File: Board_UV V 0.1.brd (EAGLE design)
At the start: 100 x 80 mm, 32 parts, among them IC4 74HC14D, IC5 MAX3232CSE, U1 TLP521-4(GB), U2 TLP521-4(GB), U3 TLP521-4(GB)

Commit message: Add other component
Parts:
- added JP1, JP2: (no value), pinhead:1X08
- added JP3: (no value), pinhead:1X02
- added JP4: (no value), pinhead:1X16
- added JP5: (no value), pinhead:1X04
- added JP6: (no value), pinhead:1X06
- added JP7: (no value), pinhead:1X12
- added JP8: (no value), pinhead:1X03
- added LS1: BUZZER-PTH_KIT, SparkFun-Electromechanical:BUZZER-12MM-KIT
- added Q1, Q2: 500mA/300V, SparkFun-DiscreteSemi:SOT23-3
- added R21, R22: 2k2, SparkFun-Resistors:0603
- added R23, R25, R26, R27, R28, R29: 1k, SparkFun-Resistors:0603
- added R24: 10k, SparkFun-Resistors:0603
- added R30, R31, R32, R33, R34, R35: 330, SparkFun-Resistors:0603
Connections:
- new net 1A: JP2.4
- new net 1B: JP2.3
- new net 2A: JP2.5
- new net 2B: JP2.6
- new net BTN-1: U$1.A14
- new net BTN-2: U$1.D32
- new net BTN-3: U$1.D34
- new net BTN-4: U$1.D36
- new net BTN-5: U$1.D38
- new net BUZ-12V: U$1.D13
- new net BUZ-5V: U$1.D11
- new net DHT: U$1.D7
- new net DIR: JP1.8, U$1.D45
- new net EN: JP1.1, U$1.D43
- new net LCD-D11: U$1.A8
- new net LCD-D12: U$1.A10
- new net LCD-D2: U$1.A0
- new net LCD-D3: U$1.A2
- new net LCD-D4: U$1.A4
- new net LCD-D5: U$1.A6
- new net LED-1: U$1.D40
- new net LED-2: U$1.D42
- new net LED-3: U$1.D44
- new net LED-4: U$1.D46
- new net LED-5: U$1.D48
- new net LIM-B1: U$1.D22
- new net LIM-B2: U$1.D24
- new net LIM-B3: U$1.D26
- new net LIM-B4: U$1.D28
- new net LIM-CTR: U$1.D21
- new net LIM-S1: U$1.D30
- new net LIM-S2: U$1.D31
- new net MISO: JP1.2, U$1.D50
- new net MOSI: JP1.5, U$1.D51
- new net N$101: JP8.3
- new net N$25: Q1.1, R21.1
- new net N$41: R21.2, R22.2
- new net N$42: LS1.-, Q1.3
- new net N$66: Q2.1, R22.1
- new net N$67: JP3.2
- new net N$68: Q2.3
- new net N$69: R24.2, U2.5
- new net N$70: JP6.6, R25.1
- new net N$71: JP4.3, R23.1
- new net N$72: JP4.4
- new net N$73: JP5.2
- new net N$74: JP4.6
- new net N$75: JP5.3
- new net N$76: JP6.5, R26.1
- new net N$77: JP4.14
- new net N$78: JP4.13
- new net N$79: JP4.12
- new net N$80: JP4.11
- new net N$81: JP6.4, R27.1
- new net N$82: JP6.3, R28.1
- new net N$83: JP6.2, R29.1
- new net N$84: U2.12
- new net N$85: JP7.7, R33.2
- new net N$86: R24.1
- new net N$87: JP7.1, R30.2
- new net N$88: JP7.2
- new net N$89: JP7.3, R31.2
- new net N$90: JP7.4
- new net N$91: JP7.5, R32.2
- new net N$92: JP7.6
- new net N$93: JP7.8
- new net N$94: JP7.9, R34.2
- new net N$95: JP7.10
- new net N$96: JP7.11, R35.2
- new net N$97: JP7.12
- new net RL-1: U$1.D23
- new net RL-2: U$1.D25
- new net RL-3: U$1.D27
- new net RL-4: U$1.D29
- new net RX-DB9: U$1.D17
- new net RX-PWR: U$1.D19
- new net SCK: JP1.3, U$1.D52
- new net SPDT-1: U$1.D33
- new net SPDT-2: U$1.D35
- new net SPDT-3: U$1.D37
- new net SPDT-4: U$1.D39
- new net SPDT-5: U$1.D41
- new net SS: JP1.4, U$1.D53
- new net STEP: JP1.7, U$1.D49
- new net TX-DB9: U$1.D16
- new net TX-PWR: U$1.D18
- net GND: now also JP2.1, JP4.1, JP4.16, JP4.5, JP5.4, JP8.1, Q1.2, Q2.2, R25.2, R26.2, R27.2, R28.2, R29.2, U$1.GND.1, U$1.GND.2, U2.11
- net GND-ISO: now also JP2.7, U2.6
- net VCC: now also JP2.2, JP4.15, JP4.2, JP5.1, JP6.1, JP8.2, LS1.+, R23.2, R30.1, R31.1, R32.1, R33.1, R34.1, R35.1, U$1.+5V.1, U$1.+5V.2, U$1.VIN.1, U$1.VIN.2
- net VCC_2: now also JP2.8, JP3.1

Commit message: add board design
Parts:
- removed JP3: (no value), pinhead:1X02
- removed JP4: (no value), pinhead:1X16
- removed JP5: (no value), pinhead:1X04
- removed JP6: (no value), pinhead:1X06
- removed JP7: (no value), pinhead:1X12
- removed JP8: (no value), pinhead:1X03
- added DS1: LCM-S02004DSF, LCM-S02004DSF:LCMS02004DSF
- added H1, H2, H3, H4: MOUNT-PAD-SQUARE3.0, holes:3,0-PAD-SQUARE
- added IC1: 74HC14D, 74xx-eu:SO14
- added J2: POWER_JACK, SparkFun-Connectors:POWER_JACK_PTH
- added LED1, LED2, LED3, LED4, LED5, LED6: (no value), led:LED5MM
- added R36, R37, R38, R39, R41, R42: 1k, SparkFun-Resistors:0603
- added S1, S2, S3, S4, S5: MOMENTARY-SWITCH-SPST-PTH-12MM, SparkFun-Switches:TACTILE_SWITCH_PTH_12MM
- added U$2, U$3, U$4, U$5, U$6, U$7: ROCKER, rocker sw:320-916
- added U$8: DC-DC-STEP-DOWN-LM2596, diy-modules:DC-DC-STEP-DOWN-LM2596
- added X1: 22-23-2021, con-molex:22-23-2021
- added X2: 1751303, con-phoenix-350:1751303
- added X3: 1751277, con-phoenix-350:1751277
- added X4: 22-23-2031, con-molex:22-23-2031
- added X5: 22-23-2041, con-molex:22-23-2041
- added X6: 1751280, con-phoenix-350:1751280
- R23: value 1k -> 10k
- moved R31 350.4 mm to (130.7, 76.2)
- moved R24 317.5 mm to (146.2, 65.3), flipped to the bottom
- moved R33 300.8 mm to (117.9, 15.3)
- moved R26 294.1 mm to (21.1, 96.8), turned to 180 degrees
- moved R25 292.9 mm to (21.1, 99.2), turned to 180 degrees
- moved R29 290.9 mm to (99.1, 39.5), turned to 90 degrees
- moved R28 289.2 mm to (101.1, 39.5), turned to 90 degrees
- moved R35 287.6 mm to (41.9, 40.6), turned to 270 degrees
- moved R34 285.2 mm to (44.5, 40.6), turned to 270 degrees
- moved Q2 282.9 mm to (129.0, 56.3), flipped to the bottom, turned to 90 degrees
- moved R27 282.1 mm to (94.5, 39.5), turned to 270 degrees
- moved R32 280.6 mm to (49.5, 40.6), turned to 270 degrees
- moved R22 276.7 mm to (125.5, 56.2), flipped to the bottom, turned to 90 degrees
- moved R30 272.6 mm to (47.0, 40.6), turned to 270 degrees
- moved R23 260.1 mm to (84.6, 53.6), flipped to the bottom, turned to 90 degrees
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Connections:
- removed net N$101: JP8.3
- removed net N$11: R1.2
- removed net N$12: IC4.1, R2.2, U1.16
- removed net N$17: IC4.3, R3.2, U1.14
- removed net N$18: IC4.5, R5.1, U1.12
- removed net N$19: IC4.13, R6.1, U1.10
- removed net N$20: R4.1
- removed net N$21: R7.1
- removed net N$22: R8.1
- removed net N$26: R9.2
- removed net N$27: IC4.11, R10.2, U2.16
- removed net N$28: IC4.9, R11.2, U2.14
- removed net N$29: R13.1, U3.1
- removed net N$30: U3.15
- removed net N$31: U3.13
- removed net N$32: U3.11
- removed net N$34: U3.9
- removed net N$35: R16.2, U3.3
- removed net N$36: R19.2, U3.5
- removed net N$40: R12.1
- removed net N$41: R21.2, R22.2
- removed net N$43: R20.2, U3.7
- removed net N$44: IC4.8
- removed net N$45: IC4.10
- removed net N$46: IC4.12
- removed net N$50: IC4.2
- removed net N$51: IC4.4
- removed net N$52: IC4.6
- removed net N$67: JP3.2
- removed net N$68: Q2.3
- removed net N$70: JP6.6, R25.1
- removed net N$71: JP4.3, R23.1
- removed net N$72: JP4.4
- removed net N$73: JP5.2
- removed net N$74: JP4.6
- removed net N$75: JP5.3
- removed net N$76: JP6.5, R26.1
- removed net N$77: JP4.14
- removed net N$78: JP4.13
- removed net N$79: JP4.12
- removed net N$80: JP4.11
- removed net N$81: JP6.4, R27.1
- removed net N$82: JP6.3, R28.1
- removed net N$83: JP6.2, R29.1
- removed net N$84: U2.12
- removed net N$85: JP7.7, R33.2
- removed net N$86: R24.1
- removed net N$87: JP7.1, R30.2
- removed net N$88: JP7.2
- removed net N$90: JP7.4
- removed net N$92: JP7.6
- removed net N$93: JP7.8
- removed net N$95: JP7.10
- removed net N$97: JP7.12
- removed net VCC_2: JP2.8, JP3.1, R13.2, R16.1, R19.1, R20.1
- new net L-IN1: IC4.13, R2.2, U1.16
- new net L-IN2: IC4.11, R3.2, U1.14
- new net L-IN3: IC4.9, R5.1, U1.12
- new net L-IN4: IC4.1, R6.1, U1.10
- new net L-IN5: IC1.13, R10.2, U2.16
- new net L-IN6: IC1.11, R11.2, U2.14
- new net L-IN7: IC1.9, R23.2, U2.12
- new net L-O1: R1.2, X2.7
- new net L-O2: R4.1, X2.6
- new net L-O3: R7.1, X2.5
- new net L-O4: R8.1, X2.4
- new net L-O5: R9.2, X2.3
- new net L-O6: R12.1, X2.2
- new net L-O7: R24.1, X2.1
- new net LED-6: LED6.A, U$1.D48
- new net N$47: Q2.3, X1.2
- new net N$56: DS1.3, R36.1
- new net R-O1: U3.15, X3.5
- new net R-O2: U3.13, X3.4
- new net R-O3: U3.11, X3.3
- new net R-O4: U3.9, X3.2
- new net VCC-ISO: J2.PWR, JP2.8, R14.1, R15.1, R17.2, R18.2, U$8.IN+, X1.1, X2.8, X6.1
- new net VO-STEP: U$7.P$1, U$8.OUT+
- net 1A: now also X6.5
- net 1B: now also JP2.5, X6.4; no longer JP2.3
- net 2A: now also JP2.3, X6.6; no longer JP2.5
- net 2B: now also X6.3
- net BTN-1: now also R29.1, S5.3, U$1.D34; no longer U$1.A14
- net BTN-2: now also R28.1, S4.3, U$1.D36; no longer U$1.D32
- net BTN-3: now also R27.1, S3.3, U$1.D32; no longer U$1.D34
- net BTN-4: now also R26.1, S2.3, U$1.D3; no longer U$1.D36
- net BTN-5: now also R25.1, S1.3, U$1.D5; no longer U$1.D38
- net BUZ-12V: now also R22.2
- net BUZ-5V: now also R21.2
- net DHT: now also X4.3
- net GND: now also DS1.1, DS1.16, DS1.5, IC1.7, R37.2, R38.2, R39.2, R41.2, R42.2, U$8.OUT-, X4.1, X5.4; no longer JP4.1, JP4.16, JP4.5, JP5.4, JP8.1, Q2.2
- net GND-ISO: now also J2.GND, J2.GNDBREAK, Q2.2, U$8.IN-, X3.1, X6.2
- net LCD-D11: now also DS1.13, U$1.D10; no longer U$1.A8
- net LCD-D12: now also DS1.14, U$1.D12; no longer U$1.A10
- net LCD-D2: now also DS1.4, U$1.D2; no longer U$1.A0
- net LCD-D3: now also DS1.6, U$1.D4; no longer U$1.A2
- net LCD-D4: now also DS1.11, U$1.D6; no longer U$1.A4
- net LCD-D5: now also DS1.12, U$1.D8; no longer U$1.A6
- net LED-1: now also LED1.A
- net LED-2: now also LED2.A
- net LED-3: now also LED3.A
- net LED-4: now also LED4.A
- net LED-5: now also LED5.A, U$1.D47; no longer U$1.D48
- net LIM-B1: now also IC4.12, U$1.D31; no longer U$1.D22
- net LIM-B2: now also IC4.10, U$1.D30; no longer U$1.D24
- net LIM-B3: now also IC4.8, U$1.D28; no longer U$1.D26
- net LIM-B4: now also IC4.2, U$1.D26; no longer U$1.D28
- net LIM-CTR: now also IC1.8
- net LIM-S1: now also IC1.12, U$1.D24; no longer U$1.D30
- net LIM-S2: now also IC1.10, U$1.D22; no longer U$1.D31
- net N$8: now also LED1.K, R30.2; no longer IC5.11
- net N$89: now also LED2.K; no longer JP7.3
- net N$9: now also LED4.K, R33.2; no longer IC5.12
- net N$91: now also LED3.K; no longer JP7.5
- net N$94: now also LED5.K; no longer JP7.9
- net N$96: now also LED6.K; no longer JP7.11
- net RL-1: now also R13.1, U3.1
- net RL-2: now also R16.2, U3.3
- net RL-3: now also R19.2, U$1.D29, U3.5; no longer U$1.D27
- net RL-4: now also R20.2, U$1.D27, U3.7; no longer U$1.D29
- net RX-DB9: now also IC5.12
- net RX-PWR: now also X5.3
- net SPDT-1: now also R39.1, U$2.P$2
- net SPDT-2: now also R37.1, U$3.P$2
- net SPDT-3: now also R42.1, U$4.P$2
- net SPDT-4: now also R38.1, U$5.P$2
- net SPDT-5: now also R41.1, U$6.P$2
- net TX-DB9: now also IC5.11
- net TX-PWR: now also X5.2
- net VCC: now also DS1.15, DS1.2, IC1.14, R13.2, R16.1, R19.1, R20.1, R23.1, R36.2, S1.1, S2.1, S3.1, S4.1, S5.1, U$2.P$1, U$3.P$1, U$4.P$1, U$5.P$1, U$6.P$1, U$7.P$2, X4.2, X5.1; no longer JP4.15, JP4.2, JP5.1, JP6.1, JP8.2, R14.1, R15.1, R17.2, R18.2, R23.2
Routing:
- net VCC: track 0.00 -> 805.4 mm, vias 0 -> 4
- net VCC-ISO: track 0.00 -> 176.4 mm
- net GND-ISO: track 0.00 -> 135.6 mm
- net GND: track 0.00 -> 130.8 mm, vias 0 -> 8
- net LIM-CTR: track 0.00 -> 120.7 mm, vias 0 -> 3
- net SPDT-1: track 0.00 -> 115.9 mm
- net BUZ-12V: track 0.00 -> 114.0 mm, vias 0 -> 1
- net BTN-3: track 0.00 -> 113.6 mm
- net RL-1: track 0.00 -> 108.9 mm, vias 0 -> 1
- net RX-DB9: track 0.00 -> 98.1 mm, vias 0 -> 2
- net RL-2: track 0.00 -> 94.4 mm, vias 0 -> 1
- net TX-DB9: track 0.00 -> 93.8 mm, vias 0 -> 2
- net BTN-2: track 0.00 -> 91.7 mm
- net DHT: track 0.00 -> 87.1 mm
- net LED-6: track 0.00 -> 86.8 mm
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- added copper zone on layer 1, net GND
- added copper zone on layer 16, net GND
- added copper zone on layer 16, net GND-ISO
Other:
- board size 100 x 80 mm -> 160.2 x 107.5 mm

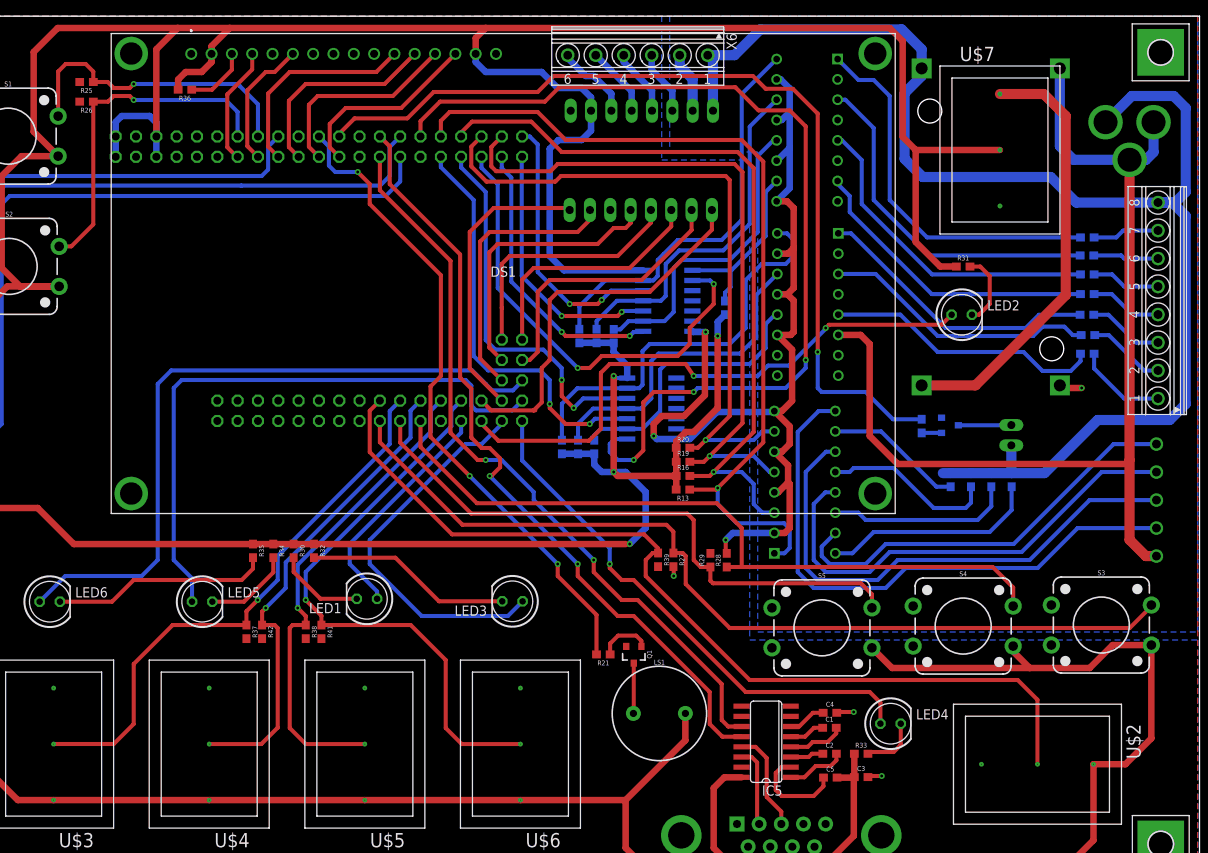
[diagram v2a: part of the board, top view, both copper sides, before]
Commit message: change button power reset
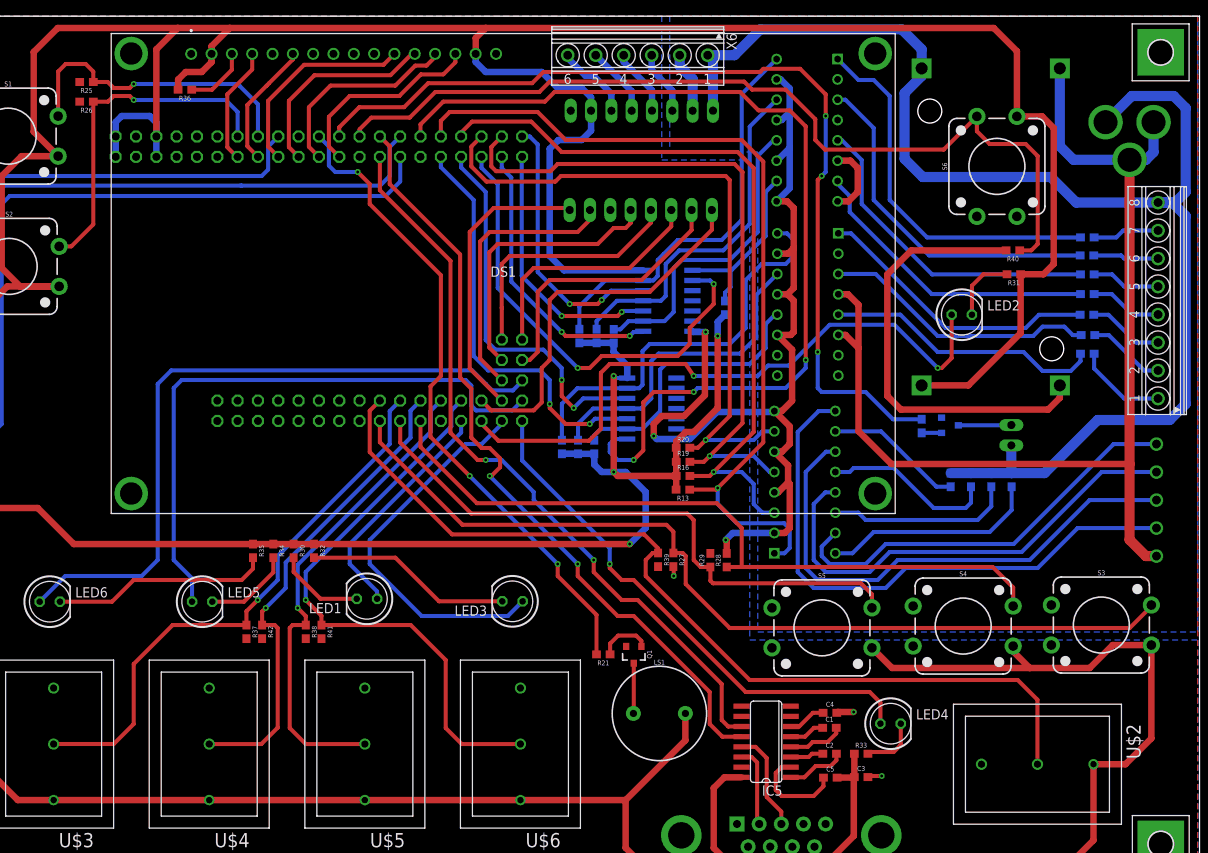
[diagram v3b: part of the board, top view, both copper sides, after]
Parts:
- removed U$7: ROCKER, rocker sw:320-916
- added R40: 1k, SparkFun-Resistors:0603
- added S6: MOMENTARY-SWITCH-SPST-PTH-12MM, SparkFun-Switches:TACTILE_SWITCH_PTH_12MM
- moved R31 6.40 mm to (137.0, 75.2), turned to 180 degrees
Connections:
- removed net VO-STEP: U$7.P$1, U$8.OUT+
- new net RST: R40.1, S6.3, U$1.D15
- net GND: now also R40.2
- net VCC: now also S6.1, U$8.OUT+; no longer U$7.P$2
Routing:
- net RST: track 0.00 -> 111.6 mm
- net VO-STEP: track 54.4 -> 0.00 mm
- net GND: track 130.8 -> 183.7 mm, vias 8 -> 7
- net VCC: track 805.4 -> 835.4 mm
- net GND-ISO: track 135.6 -> 152.2 mm
- net LED-2: track 72.1 -> 79.7 mm
- net BUZ-12V: track 114.0 -> 118.0 mm, vias 1 -> 3
- net LCD-D12: track 23.9 -> 25.2 mm
- net 2A: track 10.9 -> 9.78 mm
- net VCC-ISO: track 176.4 -> 175.5 mm
- net LIM-CTR: track 120.7 -> 120.0 mm
- net LCD-D3: track 16.4 -> 15.8 mm
- net N$89: track 9.23 -> 8.60 mm
- net LCD-D4: track 26.3 -> 25.7 mm

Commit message: finalisasi and add name
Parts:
- removed J2: POWER_JACK, SparkFun-Connectors:POWER_JACK_PTH
- added X7: 1751248, con-phoenix-350:1751248
- moved J1 2.50 mm to (108.0, 7.58)
- moved X6 0.50 mm to (90.0, 103.0), flipped to the bottom, turned to 0 degrees
- moved X2 0.12 mm to (155.1, 71.9), flipped to the bottom
- renumbered S1 to BUTTON1, S2 to BUTTON2, S3 to BUTTON5, S4 to BUTTON4, S5 to BUTTON3, S6 to BUTTON6, U$2 to SWITCH5, U$3 to SWITCH1, U$4 to SWITCH2, U$5 to SWITCH3, U$6 to SWITCH4
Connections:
- net GND-ISO: now also X7.1; no longer J2.GND, J2.GNDBREAK
- net VCC-ISO: now also X7.2; no longer J2.PWR
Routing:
- net VCC-ISO: track 175.5 -> 162.8 mm
- net GND-ISO: track 152.2 -> 148.6 mm
- net N$10: track 12.7 -> 10.2 mm
- net N$6: track 10.0 -> 7.68 mm
- net N$7: track 12.2 -> 10.1 mm
- net GND: track 183.7 -> 184.6 mm
- net N$38: track 21.5 -> 22.3 mm
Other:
- board text added: "+12V"
- board text added: "1A"
- board text added: "1B"
- board text added: "2A"
- board text added: "2B"
- board text added: "BUZZER"
- board text added: "DHT"
- board text added: "DIR"
- board text added: "GND"
- board text added: "LIM1"
- board text added: "LIM2"
- board text added: "LIM3"
- board text added: "LIM4"
- board text added: "LIM5"
- board text added: "LIM6"
- board text added: "LIM7"
- board text added: "RL1"
- board text added: "RL2"
- board text added: "RL3"
- board text added: "RL4"
- board text added: "RX"
- board text added: "TX"
- board text added: "VCC"

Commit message: last update
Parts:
- moved C3 17.8 mm to (100.1, 13.0), turned to 90 degrees
- moved C4 1.39 mm to (113.3, 19.2)
- moved C1 1.30 mm to (113.3, 17.4)
- moved C2 0.72 mm to (113.4, 14.9)
- moved C5 0.67 mm to (113.5, 12.0)
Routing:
- net VCC: track 835.1 -> 820.3 mm
- net N$6: track 7.68 -> 10.3 mm
- net GND: track 184.6 -> 187.0 mm
- net RL-3: track 85.6 -> 83.7 mm
- net TX-PWR: track 85.4 -> 83.6 mm
- net GND-ISO: track 148.6 -> 150.4 mm
- net RX-PWR: track 84.8 -> 83.1 mm
- net DIR: track 36.6 -> 34.9 mm
- net STEP: track 34.5 -> 33.0 mm
- net MOSI: track 34.9 -> 33.6 mm
- net BTN-1: track 75.1 -> 73.9 mm
- net N$2: track 4.77 -> 3.57 mm
- net N$1: track 4.46 -> 3.30 mm
- net RL-4: track 83.0 -> 81.9 mm
- net N$5: track 7.10 -> 6.00 mm
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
